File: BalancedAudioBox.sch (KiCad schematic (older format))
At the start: 3 parts, among them J1 Conn_02x10_Odd_Even, J2 Conn_01x01

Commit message: selecting actual components
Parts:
- removed J2: Conn_01x01, symbol Connector_Generic:Conn_01x01
- added J?: Conn_01x02, symbol Connector_Generic:Conn_01x02
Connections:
- wire segments 26 -> 29
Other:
- note added: "max 200mA limited by TPS61252"
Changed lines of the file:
@@
 EESchema Schematic File Version 4
+LIBS:BalancedAudioBox-cache
 EELAYER 29 0
 EELAYER END
@@
 F0 "PowerSupply" 50
 F1 "PowerSupply.sch" 50
+F2 "VIN" I L 4600 5950 50
 $EndSheet
 $Sheet
@@
 	6300 2150 7450 2150
 $Comp
-L Connector_Generic:Conn_01x01 J2
-U 1 1 5D44CB93
-P 3200 5950
-F 0 "J2" H 3118 5725 50  0000 C CNN
-F 1 "Conn_01x01" H 3118 5816 50  0000 C CNN
-F 2 "" H 3200 5950 50  0001 C CNN
-F 3 "~" H 3200 5950 50  0001 C CNN
-	1    3200 5950
-	-1   0    0    1
-$EndComp
-$Comp
 L Jumper:SolderJumper_3_Bridged12 JP3
 U 1 1 5D47A7E1
@@
 Wire Wire Line
 	3850 1700 3850 1500
+$Comp
+L Connector_Generic:Conn_01x02 J?
+U 1 1 5D40F023
+P 2950 5950
+F 0 "J?" H 2868 6167 50  0000 C CNN
+F 1 "Conn_01x02" H 2868 6076 50  0000 C CNN
+F 2 "" H 2950 5950 50  0001 C CNN
+F 3 "~" H 2950 5950 50  0001 C CNN
+	1    2950 5950
+	-1   0    0    -1
+$EndComp
+Wire Wire Line
+	3150 5950 4600 5950
+$Comp
+L power:GND #PWR?
+U 1 1 5D40FB13
+P 3300 6250
+F 0 "#PWR?" H 3300 6000 50  0001 C CNN
+F 1 "GND" H 3305 6077 50  0000 C CNN
+F 2 "" H 3300 6250 50  0001 C CNN
+F 3 "" H 3300 6250 50  0001 C CNN
+	1    3300 6250
+	1    0    0    -1
+$EndComp
+Wire Wire Line
+	3150 6050 3300 6050
+Wire Wire Line
+	3300 6050 3300 6250
+Text Notes 3150 5650 0    50   ~ 0
+max 200mA limited by TPS61252
 $EndSCHEMATC

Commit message: work
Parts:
- J2: renamed from J?; footprint (none) -> Connector_PinSocket_2.54mm:PinSocket_1x01_P2.54mm_Vertical
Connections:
- no-connect marks 0 -> 7
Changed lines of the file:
@@
 F1 "OutputDriver.sch" 50
 F2 "LEFT" I L 7450 2150 50
+F3 "RIGHT" I L 7450 2250 50
 $EndSheet
 $Sheet
@@
 	3850 1700 3850 1500
 $Comp
-L Connector_Generic:Conn_01x02 J?
+L Connector_Generic:Conn_01x02 J2
 U 1 1 5D40F023
 P 2950 5950
-F 0 "J?" H 2868 6167 50  0000 C CNN
+F 0 "J2" H 2868 6167 50  0000 C CNN
 F 1 "Conn_01x02" H 2868 6076 50  0000 C CNN
-F 2 "" H 2950 5950 50  0001 C CNN
+F 2 "Connector_PinSocket_2.54mm:PinSocket_1x01_P2.54mm_Vertical" H 2950 5950 50  0001 C CNN
 F 3 "~" H 2950 5950 50  0001 C CNN
 	1    2950 5950
@@
 	3150 5950 4600 5950
 $Comp
-L power:GND #PWR?
+L power:GND #PWR049
 U 1 1 5D40FB13
 P 3300 6250
-F 0 "#PWR?" H 3300 6000 50  0001 C CNN
+F 0 "#PWR049" H 3300 6000 50  0001 C CNN
 F 1 "GND" H 3305 6077 50  0000 C CNN
 F 2 "" H 3300 6250 50  0001 C CNN
@@
 Text Notes 3150 5650 0    50   ~ 0
 max 200mA limited by TPS61252
+NoConn ~ 2200 2800
+NoConn ~ 2200 2900
+NoConn ~ 2200 2000
+NoConn ~ 2200 2100
+NoConn ~ 2200 2200
+NoConn ~ 2200 2300
+NoConn ~ 2200 2400
+Wire Wire Line
+	6300 2250 7450 2250
 $EndSCHEMATC

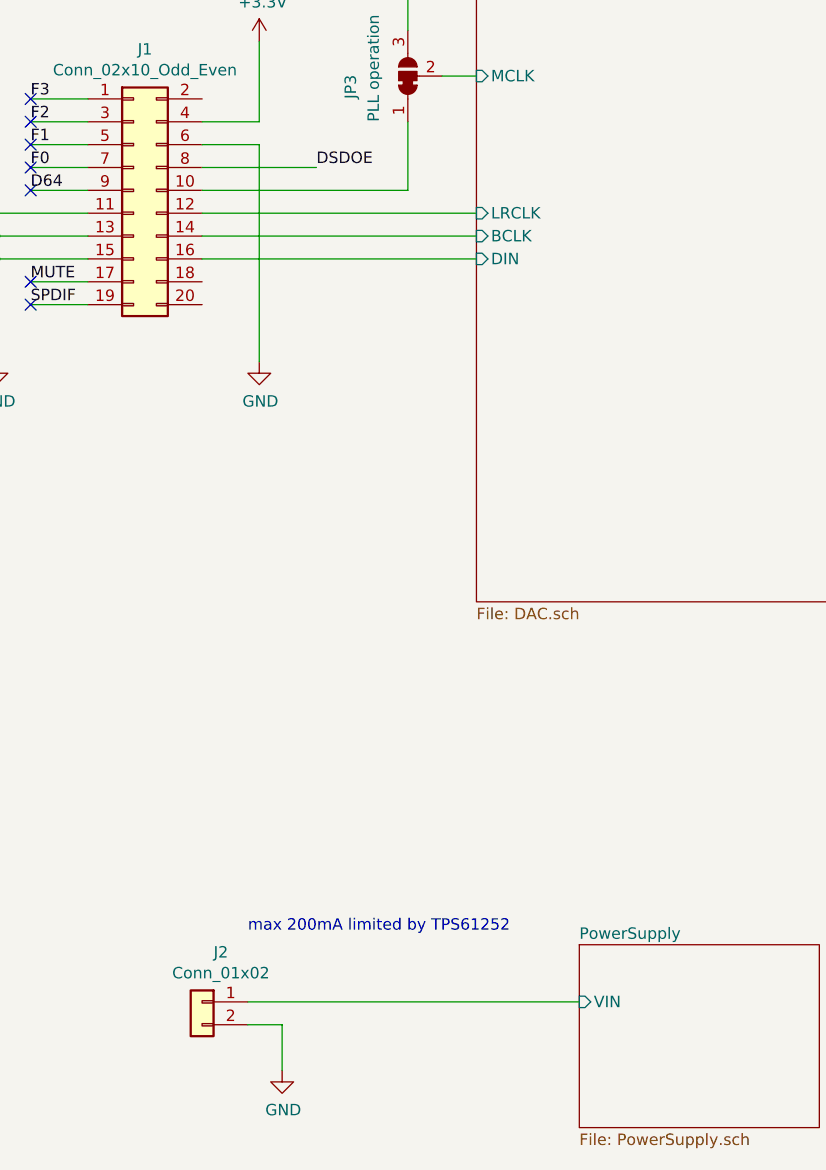
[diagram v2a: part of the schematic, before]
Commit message: adding PCB libraries
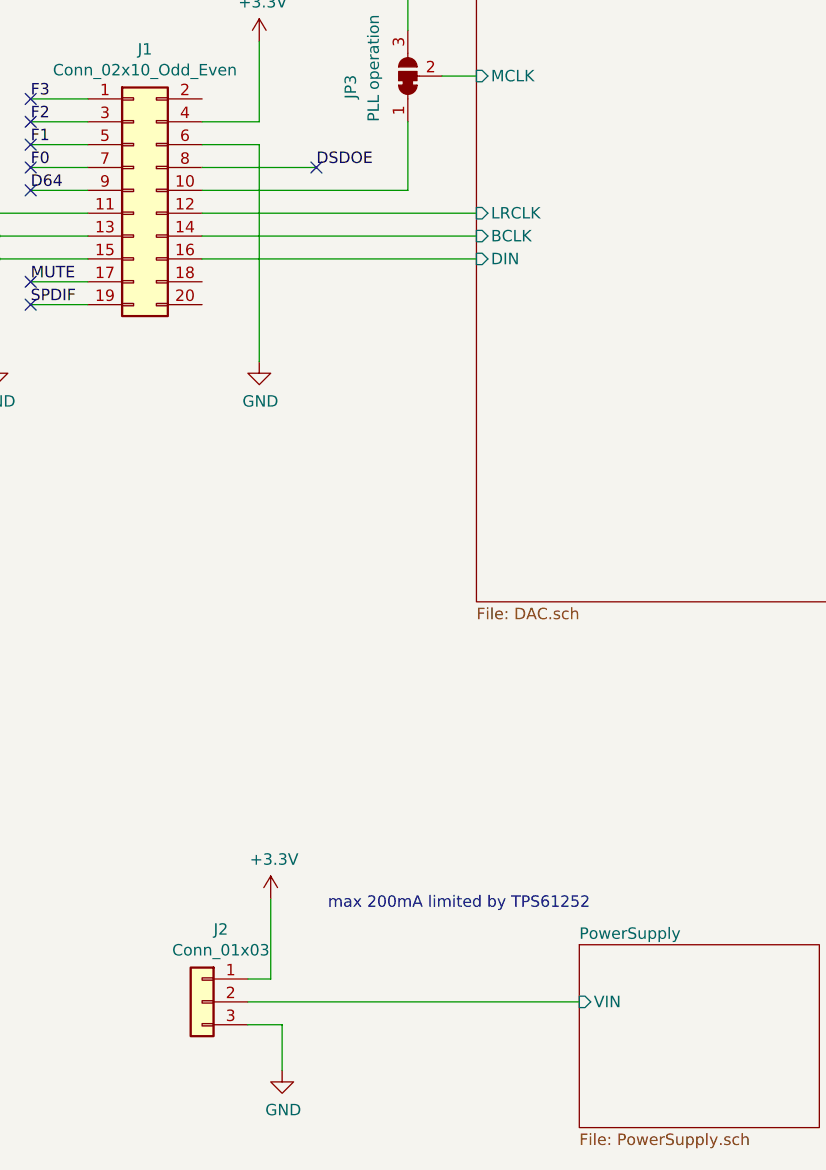
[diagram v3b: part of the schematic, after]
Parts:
- removed J2: Conn_01x02, Connector_PinSocket_2.54mm:PinSocket_1x01_P2.54mm_Vertical, symbol Connector_Generic:Conn_01x02
- added J2: Conn_01x03, Connector_PinHeader_2.54mm:PinHeader_1x01_P2.54mm_Vertical, symbol Connector_Generic:Conn_01x03
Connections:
- net +3V3: now also J2.1 (Pin_1)
- net GND: now also J2.3 (Pin_3)
- net PowerSupply/VIN: now also J2.2 (Pin_2)
- no-connect marks 7 -> 8
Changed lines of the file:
@@
 Wire Wire Line
 	3850 1700 3850 1500
-$Comp
-L Connector_Generic:Conn_01x02 J2
-U 1 1 5D40F023
-P 2950 5950
-F 0 "J2" H 2868 6167 50  0000 C CNN
-F 1 "Conn_01x02" H 2868 6076 50  0000 C CNN
-F 2 "Connector_PinSocket_2.54mm:PinSocket_1x01_P2.54mm_Vertical" H 2950 5950 50  0001 C CNN
-F 3 "~" H 2950 5950 50  0001 C CNN
-	1    2950 5950
-	-1   0    0    -1
-$EndComp
 Wire Wire Line
 	3150 5950 4600 5950
@@
 Wire Wire Line
 	3300 6050 3300 6250
-Text Notes 3150 5650 0    50   ~ 0
+Text Notes 3500 5550 0    50   ~ 0
 max 200mA limited by TPS61252
 NoConn ~ 2200 2800
@@
 Wire Wire Line
 	6300 2250 7450 2250
+NoConn ~ 3450 2300
+$Comp
+L Connector_Generic:Conn_01x03 J2
+U 1 1 5D436D81
+P 2950 5950
+F 0 "J2" H 2868 6267 50  0000 C CNN
+F 1 "Conn_01x03" H 2868 6176 50  0000 C CNN
+F 2 "Connector_PinHeader_2.54mm:PinHeader_1x01_P2.54mm_Vertical" H 2950 5950 50  0001 C CNN
+F 3 "~" H 2950 5950 50  0001 C CNN
+	1    2950 5950
+	-1   0    0    -1
+$EndComp
+$Comp
+L power:+3.3V #PWR0101
+U 1 1 5D437E68
+P 3250 5500
+F 0 "#PWR0101" H 3250 5350 50  0001 C CNN
+F 1 "+3.3V" H 3265 5673 50  0000 C CNN
+F 2 "" H 3250 5500 50  0001 C CNN
+F 3 "" H 3250 5500 50  0001 C CNN
+	1    3250 5500
+	1    0    0    -1
+$EndComp
+Wire Wire Line
+	3150 5850 3250 5850
+Wire Wire Line
+	3250 5850 3250 5500
 $EndSCHEMATC

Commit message: ps checked
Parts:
- added J?: Conn_01x03, Connector_PinHeader_2.54mm:PinHeader_1x01_P2.54mm_Vertical, symbol Connector_Generic:Conn_01x03
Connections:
- net GND: now also J?.2 (Pin_2)
- new net +5V: J?.1 (Pin_1)
- new net -5V: J?.3 (Pin_3)
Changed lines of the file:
@@
 Wire Wire Line
 	3250 5850 3250 5500
+$Comp
+L Connector_Generic:Conn_01x03 J?
+U 1 1 5D431850
+P 7950 5550
+F 0 "J?" H 7868 5867 50  0000 C CNN
+F 1 "Conn_01x03" H 7868 5776 50  0000 C CNN
+F 2 "Connector_PinHeader_2.54mm:PinHeader_1x01_P2.54mm_Vertical" H 7950 5550 50  0001 C CNN
+F 3 "~" H 7950 5550 50  0001 C CNN
+	1    7950 5550
+	-1   0    0    -1
+$EndComp
+$Comp
+L power:GND #PWR?
+U 1 1 5D431EC6
+P 8500 6050
+F 0 "#PWR?" H 8500 5800 50  0001 C CNN
+F 1 "GND" H 8505 5877 50  0000 C CNN
+F 2 "" H 8500 6050 50  0001 C CNN
+F 3 "" H 8500 6050 50  0001 C CNN
+	1    8500 6050
+	1    0    0    -1
+$EndComp
+$Comp
+L power:+5V #PWR?
+U 1 1 5D434681
+P 8500 5250
+F 0 "#PWR?" H 8500 5100 50  0001 C CNN
+F 1 "+5V" H 8515 5423 50  0000 C CNN
+F 2 "" H 8500 5250 50  0001 C CNN
+F 3 "" H 8500 5250 50  0001 C CNN
+	1    8500 5250
+	1    0    0    -1
+$EndComp
+$Comp
+L power:-5V #PWR?
+U 1 1 5D434F2F
+P 8850 5250
+F 0 "#PWR?" H 8850 5350 50  0001 C CNN
+F 1 "-5V" H 8865 5423 50  0000 C CNN
+F 2 "" H 8850 5250 50  0001 C CNN
+F 3 "" H 8850 5250 50  0001 C CNN
+	1    8850 5250
+	1    0    0    -1
+$EndComp
+Wire Wire Line
+	8150 5450 8500 5450
+Wire Wire Line
+	8500 5450 8500 5250
+Wire Wire Line
+	8150 5650 8850 5650
+Wire Wire Line
+	8850 5650 8850 5250
+Wire Wire Line
+	8150 5550 8500 5550
+Wire Wire Line
+	8500 5550 8500 6050
 $EndSCHEMATC

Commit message: placement complete
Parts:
- J2: footprint Connector_PinHeader_2.54mm:PinHeader_1x01_P2.54mm_Vertical -> Connector_PinHeader_2.54mm:PinHeader_1x03_P2.54mm_Vertical
- J5: renamed from J?; footprint Connector_PinHeader_2.54mm:PinHeader_1x01_P2.54mm_Vertical -> Connector_PinHeader_2.54mm:PinHeader_1x03_P2.54mm_Vertical
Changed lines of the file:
@@
 F 0 "J2" H 2868 6267 50  0000 C CNN
 F 1 "Conn_01x03" H 2868 6176 50  0000 C CNN
-F 2 "Connector_PinHeader_2.54mm:PinHeader_1x01_P2.54mm_Vertical" H 2950 5950 50  0001 C CNN
+F 2 "Connector_PinHeader_2.54mm:PinHeader_1x03_P2.54mm_Vertical" H 2950 5950 50  0001 C CNN
 F 3 "~" H 2950 5950 50  0001 C CNN
 	1    2950 5950
@@
 	3250 5850 3250 5500
 $Comp
-L Connector_Generic:Conn_01x03 J?
+L Connector_Generic:Conn_01x03 J5
 U 1 1 5D431850
 P 7950 5550
-F 0 "J?" H 7868 5867 50  0000 C CNN
+F 0 "J5" H 7868 5867 50  0000 C CNN
 F 1 "Conn_01x03" H 7868 5776 50  0000 C CNN
-F 2 "Connector_PinHeader_2.54mm:PinHeader_1x01_P2.54mm_Vertical" H 7950 5550 50  0001 C CNN
+F 2 "Connector_PinHeader_2.54mm:PinHeader_1x03_P2.54mm_Vertical" H 7950 5550 50  0001 C CNN
 F 3 "~" H 7950 5550 50  0001 C CNN
 	1    7950 5550
@@
 $EndComp
 $Comp
-L power:GND #PWR?
+L power:GND #PWR070
 U 1 1 5D431EC6
 P 8500 6050
-F 0 "#PWR?" H 8500 5800 50  0001 C CNN
+F 0 "#PWR070" H 8500 5800 50  0001 C CNN
 F 1 "GND" H 8505 5877 50  0000 C CNN
 F 2 "" H 8500 6050 50  0001 C CNN
@@
 $EndComp
 $Comp
-L power:+5V #PWR?
+L power:+5V #PWR069
 U 1 1 5D434681
 P 8500 5250
-F 0 "#PWR?" H 8500 5100 50  0001 C CNN
+F 0 "#PWR069" H 8500 5100 50  0001 C CNN
 F 1 "+5V" H 8515 5423 50  0000 C CNN
 F 2 "" H 8500 5250 50  0001 C CNN
@@
 $EndComp
 $Comp
-L power:-5V #PWR?
+L power:-5V #PWR071
 U 1 1 5D434F2F
 P 8850 5250
-F 0 "#PWR?" H 8850 5350 50  0001 C CNN
+F 0 "#PWR071" H 8850 5350 50  0001 C CNN
 F 1 "-5V" H 8865 5423 50  0000 C CNN
 F 2 "" H 8850 5250 50  0001 C CNN

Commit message: layout and silk
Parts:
- added J7: Conn_01x05, Connector_PinHeader_2.54mm:PinHeader_1x05_P2.54mm_Vertical, symbol Connector_Generic:Conn_01x05
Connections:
- net GND: now also J7.5 (Pin_5)
- net MCLK: now reaches J1.10 (Pin_10), JP3.1 (A)
- net MCLK: now also J7.1 (Pin_1)
- net DAC/BCLK renamed BCLK
- net BCLK: now also J7.3 (Pin_3)
- net DAC/DIN renamed DIN
- net DIN: now also J7.4 (Pin_4)
- net DAC/LRCLK renamed LRCLK
- net LRCLK: now also J7.2 (Pin_2)
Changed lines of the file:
@@
 Wire Wire Line
 	8500 5550 8500 6050
+Text Label 3400 2500 0    50   ~ 0
+LRCLK
+Text Label 3400 2600 0    50   ~ 0
+BCLK
+Text Label 3400 2700 0    50   ~ 0
+DIN
+Text Label 3400 2400 0    50   ~ 0
+MCLK
+$Comp
+L Connector_Generic:Conn_01x05 J7
+U 1 1 5D4691F7
+P 3000 4300
+F 0 "J7" H 2918 4717 50  0000 C CNN
+F 1 "Conn_01x05" H 2918 4626 50  0000 C CNN
+F 2 "Connector_PinHeader_2.54mm:PinHeader_1x05_P2.54mm_Vertical" H 3000 4300 50  0001 C CNN
+F 3 "~" H 3000 4300 50  0001 C CNN
+	1    3000 4300
+	-1   0    0    -1
+$EndComp
+Text Label 3200 4100 0    50   ~ 0
+MCLK
+Text Label 3200 4200 0    50   ~ 0
+LRCLK
+Text Label 3200 4300 0    50   ~ 0
+BCLK
+Text Label 3200 4400 0    50   ~ 0
+DIN
+$Comp
+L power:GND #PWR0102
+U 1 1 5D46AD06
+P 3300 4650
+F 0 "#PWR0102" H 3300 4400 50  0001 C CNN
+F 1 "GND" H 3305 4477 50  0000 C CNN
+F 2 "" H 3300 4650 50  0001 C CNN
+F 3 "" H 3300 4650 50  0001 C CNN
+	1    3300 4650
+	1    0    0    -1
+$EndComp
+Wire Wire Line
+	3200 4500 3300 4500
+Wire Wire Line
+	3300 4500 3300 4650
 $EndSCHEMATC

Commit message: adding regulator
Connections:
- net PowerSupply/VIN renamed VIN
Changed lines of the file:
@@
 Wire Wire Line
 	3300 4500 3300 4650
+Text GLabel 3950 5950 1    50   Input ~ 0
+VIN
 $EndSCHEMATC

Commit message: more layout
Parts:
- removed J2: Conn_01x03, Connector_PinHeader_2.54mm:PinHeader_1x03_P2.54mm_Vertical, symbol Connector_Generic:Conn_01x03
- added J2: Conn_01x02, Connector_PinHeader_2.54mm:PinHeader_1x02_P2.54mm_Vertical, symbol Connector_Generic:Conn_01x02
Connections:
- net GND: now also J2.1 (Pin_1)
- net VIN: now also J2.2 (Pin_2)
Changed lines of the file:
@@
 NoConn ~ 3450 2300
-$Comp
-L Connector_Generic:Conn_01x03 J2
-U 1 1 5D436D81
-P 2950 5950
-F 0 "J2" H 2868 6267 50  0000 C CNN
-F 1 "Conn_01x03" H 2868 6176 50  0000 C CNN
-F 2 "Connector_PinHeader_2.54mm:PinHeader_1x03_P2.54mm_Vertical" H 2950 5950 50  0001 C CNN
-F 3 "~" H 2950 5950 50  0001 C CNN
-	1    2950 5950
-	-1   0    0    -1
-$EndComp
-$Comp
-L power:+3.3V #PWR0101
-U 1 1 5D437E68
-P 3250 5500
-F 0 "#PWR0101" H 3250 5350 50  0001 C CNN
-F 1 "+3.3V" H 3265 5673 50  0000 C CNN
-F 2 "" H 3250 5500 50  0001 C CNN
-F 3 "" H 3250 5500 50  0001 C CNN
-	1    3250 5500
-	1    0    0    -1
-$EndComp
-Wire Wire Line
-	3150 5850 3250 5850
-Wire Wire Line
-	3250 5850 3250 5500
 $Comp
 L Connector_Generic:Conn_01x03 J5
@@
 Text GLabel 3950 5950 1    50   Input ~ 0
 VIN
+$Comp
+L Connector_Generic:Conn_01x02 J2
+U 1 1 5D4B761F
+P 2950 6050
+F 0 "J2" H 2868 5725 50  0000 C CNN
+F 1 "Conn_01x02" H 2868 5816 50  0000 C CNN
+F 2 "Connector_PinHeader_2.54mm:PinHeader_1x02_P2.54mm_Vertical" H 2950 6050 50  0001 C CNN
+F 3 "~" H 2950 6050 50  0001 C CNN
+	1    2950 6050
+	-1   0    0    1
+$EndComp
 $EndSCHEMATC
